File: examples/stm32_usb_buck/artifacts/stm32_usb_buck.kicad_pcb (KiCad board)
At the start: 4 copper layers, 90 x 58 mm, 28 parts, among them J2 SWD 10-pin, J3 GPIO 1x4, SW1 BOOT0, U1 STM32F405RGT6, Y1 8 MHz

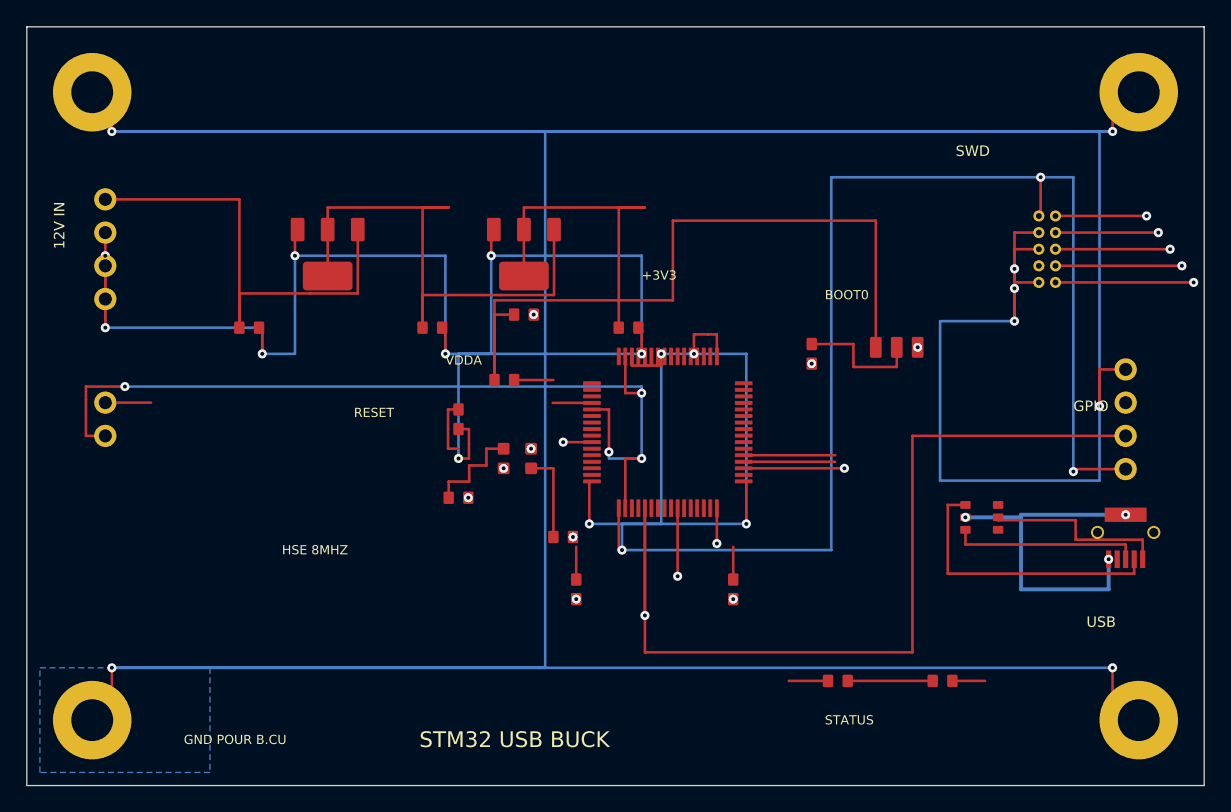
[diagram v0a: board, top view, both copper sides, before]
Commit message: Polish STM32 USB buck benchmark layout
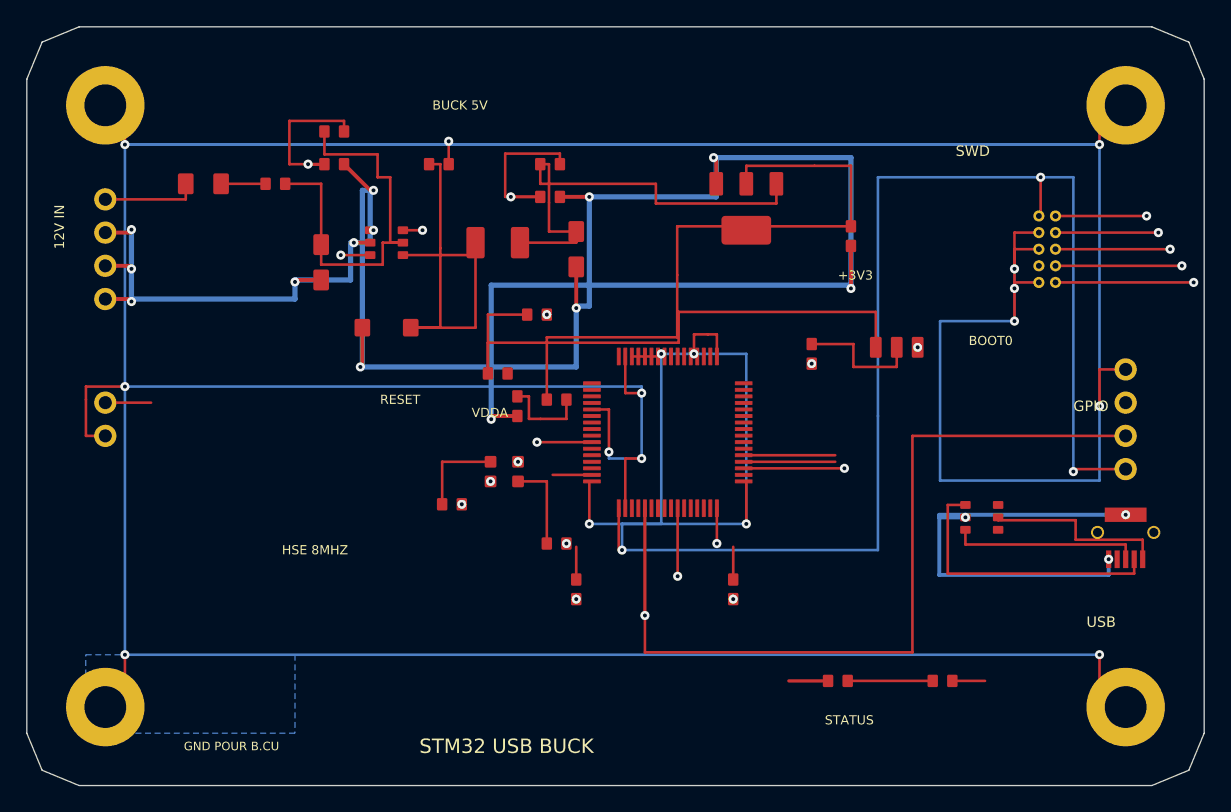
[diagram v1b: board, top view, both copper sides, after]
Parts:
- added C10: 18 pF, C_0603_1608Metric, F.Cu at (40.5, 39.5)
- added D2: Green LED, LED_0603_1608Metric, F.Cu at (70.0, 50.0)
- added H1: MountingHole_Pad, MountingHole_3.2mm_Pad_6.0mm, F.Cu at (6.00, 6.00)
- added H2: MountingHole_Pad, MountingHole_3.2mm_Pad_6.0mm, F.Cu at (84.0, 6.00)
- added H3: MountingHole_Pad, MountingHole_3.2mm_Pad_6.0mm, F.Cu at (6.00, 52.0)
- added H4: MountingHole_Pad, MountingHole_3.2mm_Pad_6.0mm, F.Cu at (84.0, 52.0)
- added J4: SWD 10-pin, PinHeader_2x05_P1.27mm_Vertical_SmallPads, F.Cu at (78.0, 17.0)
- added J5: GPIO 1x4, PinHeader_1x04_P2.54mm_Vertical, F.Cu at (84.0, 30.0)
- added R7: 330 Ohm, R_0603_1608Metric, F.Cu at (62.0, 50.0)
- added U1: STM32F405RGT6, LQFP-64_10x10mm_P0.5mm, F.Cu at (49.0, 31.0)
- C1: renamed from C4; value 100 nF -> 10 uF; footprint C_0603_1608Metric -> C_1206_3216Metric
- C2: renamed from USB/J1; value USB Micro-B -> 10 nF; footprint USB_Micro-B_Receptacle -> C_0603_1608Metric
- C3: renamed from USB/U1; value USBLC6-4SC6 -> 10 uF; footprint SOT-23-6 -> C_1206_3216Metric
- C4: renamed from SW1; value BOOT0 -> 4.7 uF; footprint SW_SPDT_PCM12 -> C_0603_1608Metric
- C5: renamed from C8; value 18 pF -> 100 nF
- C6: renamed from LED_STATUS/D; value Green LED -> 100 nF; footprint LED_0603_1608Metric -> C_0603_1608Metric
- C7: renamed from U1; value STM32F405RGT6 -> 2.2 uF; footprint LQFP-64_10x10mm_P0.5mm -> C_0603_1608Metric
- C8: renamed from J2; value SWD 10-pin -> 2.2 uF; footprint PinHeader_2x05_P1.27mm_Vertical_SmallPads -> C_0603_1608Metric
- C9: renamed from H4; value MountingHole_Pad -> 18 pF; footprint MountingHole_3.2mm_Pad_6.0mm -> C_0603_1608Metric
- D1: renamed from PWR/C3V3; value 4.7 uF -> B5819W; footprint C_0603_1608Metric -> D_SOD-123
- F1: renamed from PWR/U5; value AP1117-5.0 -> 250 mA polyfuse; footprint SOT-223-3_TabPin2 -> Fuse_1206_3216Metric
- FB1: renamed from PWR/U3V3; value AP1117-3.3 -> 600 Ohm @ 100 MHz; footprint SOT-223-3_TabPin2 -> L_0603_1608Metric
- FB2: renamed from Y1; value 8 MHz -> 600 Ohm @ 100 MHz; footprint Crystal_3225_4Pad -> L_0603_1608Metric
- J3: renamed from C9; value 18 pF -> USB Micro-B; footprint C_0603_1608Metric -> USB_Micro-B_Receptacle
- L1: renamed from PWR/C5V; value 4.7 uF -> 10 uH; footprint C_0603_1608Metric -> L_4.0x4.0mm
- R1: renamed from C5; value 100 nF -> 100 kOhm; footprint C_0603_1608Metric -> R_0603_1608Metric
- R2: renamed from C6; value 2.2 uF -> 47 kOhm; footprint C_0603_1608Metric -> R_0603_1608Metric
- R3: renamed from C7; value 2.2 uF -> 68 kOhm; footprint C_0603_1608Metric -> R_0603_1608Metric
- R4: renamed from R1; value 10 kOhm -> 15 kOhm
- R5: renamed from J3; value GPIO 1x4 -> 10 kOhm; footprint PinHeader_1x04_P2.54mm_Vertical -> R_0603_1608Metric
- R6: renamed from H1; value MountingHole_Pad -> 100 kOhm; footprint MountingHole_3.2mm_Pad_6.0mm -> R_0603_1608Metric
- SW1: renamed from H2; value MountingHole_Pad -> BOOT0; footprint MountingHole_3.2mm_Pad_6.0mm -> SW_SPDT_PCM12
- U2: renamed from PWR/CIN; value 4.7 uF -> MP2359 5V buck; footprint C_0603_1608Metric -> SOT-23-6
- U3: renamed from R2; value 100 kOhm -> AP1117-3.3; footprint R_0603_1608Metric -> SOT-223-3_TabPin2
- U4: renamed from LED_STATUS/R; value 330 Ohm -> USBLC6-4SC6; footprint R_0603_1608Metric -> SOT-23-6
- Y1: renamed from H3; value MountingHole_Pad -> 8 MHz; footprint MountingHole_3.2mm_Pad_6.0mm -> Crystal_3225_4Pad
- moved C2 59.7 mm to (31.5, 10.5), turned to 0 degrees
- moved R6 58.5 mm to (60.0, 25.0), turned to 90 degrees
- moved C9 55.0 mm to (32.5, 36.5)
- moved R5 48.1 mm to (36.0, 26.5), turned to 0 degrees
- moved J3 43.0 mm to (84.0, 39.0), turned to 180 degrees
- moved C6 41.8 mm to (39.0, 22.0)
- moved R2 37.4 mm to (23.5, 10.5), turned to 0 degrees
- moved C3 37.2 mm to (42.0, 17.0), turned to 90 degrees
- moved Y1 36.8 mm to (36.5, 34.0)
- moved R3 35.4 mm to (40.0, 10.5), turned to 0 degrees
- moved C8 35.4 mm to (54.0, 43.0), turned to 90 degrees
- moved SW1 26.9 mm to (66.5, 24.5)
- moved R1 20.2 mm to (23.5, 8.00)
- moved FB1 19.6 mm to (19.0, 12.0)
- moved D1 18.5 mm to (27.5, 23.0)
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- renumbered VIN_SRC to J1, PWR/J to J2
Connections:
- C1 pad 1: PWR/VDDA -> PWR/BUCK_IN
- C2 pad 1: USB/VBUS -> PWR/BUCK_SW
- C2 pad 2: USB/USB_DM -> PWR/BUCK_BST
- C3 pad 1: USB/USB_DP -> PWR/OUT_5V
- C3 pad 2: USB/GND -> PWR/GND
- C4 pad 1: SUPPORT/VDD -> PWR/OUT_3V3
- C4 pad 2: SUPPORT/BOOT0 -> PWR/GND
- C5 pad 1: SUPPORT/HSE_IN -> PWR/VDDA
- C5 pad 2: SUPPORT/GND -> PWR/GND
- C6 pad 1: LED_STATUS/SIGNAL -> SUPPORT/VDD
- C6 pad 2: LED_STATUS/GND -> SUPPORT/GND
- C7 pad 1: +3V3 -> SUPPORT/VCAP_1
- C7 pad 2: STATUS_LED -> SUPPORT/GND
- C8 pad 1: +3V3 -> SUPPORT/VCAP_2
- C8 pad 2: SWDIO -> SUPPORT/GND
- C9 pad 1: GND -> SUPPORT/HSE_IN
- D1 pad 1: PWR/OUT_3V3 -> PWR/GND
- D1 pad 2: PWR/GND -> PWR/BUCK_SW
- F1 pad 1: PWR/GND -> PWR/IN_12V
- F1 pad 2: PWR/OUT_5V -> PWR/FUSED_12V
- FB1 pad 1: PWR/GND -> PWR/FUSED_12V
- FB1 pad 2: PWR/OUT_3V3 -> PWR/BUCK_IN
- FB2 pad 1: SUPPORT/HSE_IN -> PWR/OUT_3V3
- FB2 pad 2: SUPPORT/GND -> PWR/VDDA
- J3 pad 1: SUPPORT/HSE_OUT -> USB/VBUS
- J3 pad 2: SUPPORT/GND -> USB/USB_DM
- L1 pad 1: PWR/OUT_5V -> PWR/BUCK_SW
- L1 pad 2: PWR/GND -> PWR/OUT_5V
- R1 pad 1: SUPPORT/VDD -> PWR/BUCK_IN
- R1 pad 2: SUPPORT/GND -> PWR/BUCK_EN
- R2 pad 1: SUPPORT/VCAP_1 -> PWR/BUCK_EN
- R2 pad 2: SUPPORT/GND -> PWR/GND
- R3 pad 1: SUPPORT/VCAP_2 -> PWR/OUT_5V
- R3 pad 2: SUPPORT/GND -> PWR/BUCK_FB
- R4 pad 1: SUPPORT/VDD -> PWR/BUCK_FB
- R4 pad 2: SUPPORT/NRST -> PWR/GND
- R5 pad 1: +3V3 -> SUPPORT/VDD
- R5 pad 2: BOOT0 -> SUPPORT/NRST
- R6 pad 1: GND -> SUPPORT/BOOT0
- SW1 pad 1: GND -> SUPPORT/VDD
- U2 pad 1: PWR/IN_12V -> PWR/BUCK_BST
- U3 pad 1: SUPPORT/BOOT0 -> PWR/GND
- U3 pad 2: SUPPORT/GND -> PWR/OUT_3V3
- U4 pad 1: LED_STATUS/SUPPLY -> USB/USB_DP
- U4 pad 2: LED_STATUS/SIGNAL -> USB/GND
- Y1 pad 1: GND -> SUPPORT/HSE_IN
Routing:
- net PWR/GND: track 121.7 -> 173.9 mm, vias 9 -> 12
- net PWR/BUCK_SW: track 0.00 -> 33.6 mm
- net PWR/BUCK_FB: track 0.00 -> 33.4 mm, vias 0 -> 2
- net PWR/BUCK_IN: track 0.00 -> 31.3 mm
- net PWR/IN_12V: track 36.6 -> 7.34 mm
- net PWR/BUCK_EN: track 0.00 -> 27.5 mm, vias 0 -> 2
- net PWR/OUT_3V3: track 25.7 -> 50.5 mm
- net PWR/BUCK_BST: track 0.00 -> 20.9 mm, vias 0 -> 2
- net SUPPORT/VDD: track 57.5 -> 44.6 mm
- net GND: track 516.8 -> 506.8 mm
- net USB/GND: track 27.0 -> 35.0 mm
- net PWR/OUT_5V: track 43.2 -> 35.6 mm
- net LED_STATUS/LED_A: track 0.00 -> 6.50 mm
- net NRST: track 103.7 -> 107.7 mm
- net LED_STATUS/SIGNAL: track 6.50 -> 2.50 mm
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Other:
- outline, holes or cut-outs redrawn
- board text added: "BUCK 5V"

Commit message: Address STM32 USB buck review findings
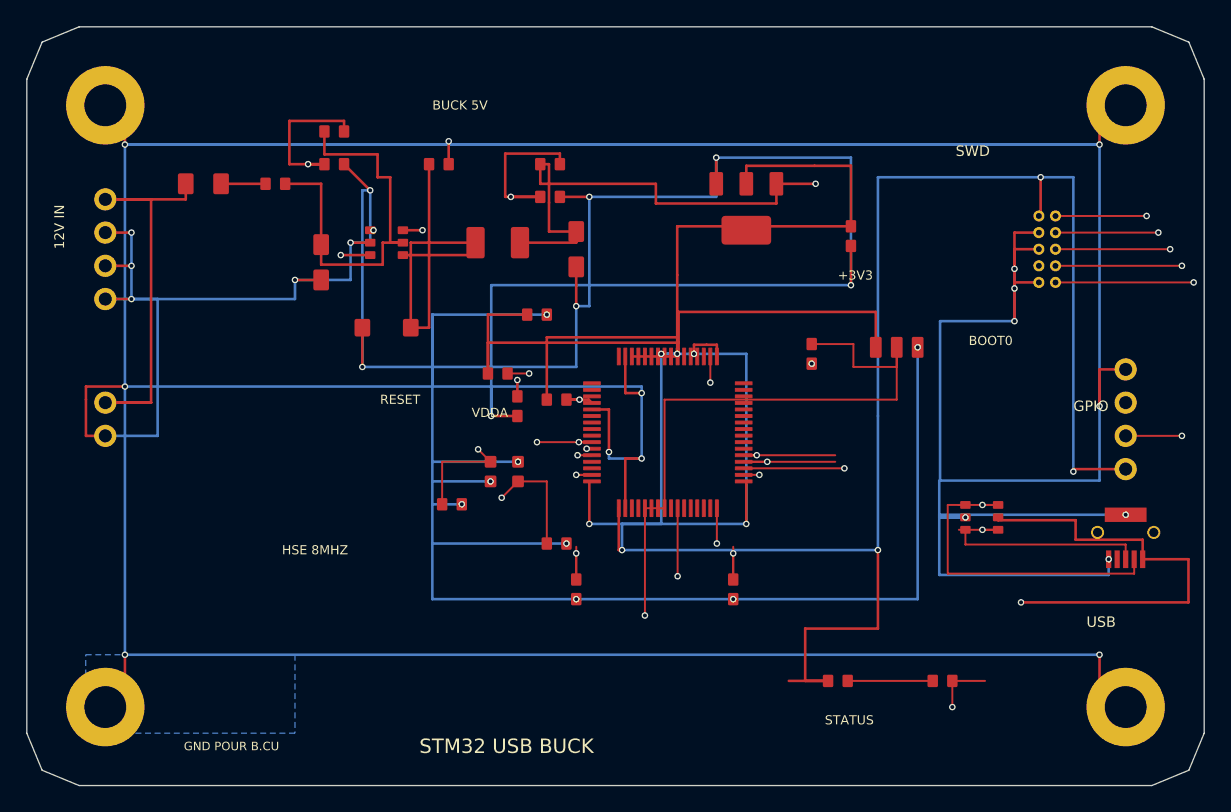
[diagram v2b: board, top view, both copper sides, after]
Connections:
- C1 pad 2: PWR/GND -> GND
- C10 pad 2: SUPPORT/GND -> GND
- C3 pad 1: PWR/OUT_5V -> +5V
- C3 pad 2: PWR/GND -> GND
- C4 pad 1: PWR/OUT_3V3 -> +3V3
- C4 pad 2: PWR/GND -> GND
- C5 pad 1: PWR/VDDA -> VDDA
- C5 pad 2: PWR/GND -> GND
- C6 pad 1: SUPPORT/VDD -> +3V3
- C6 pad 2: SUPPORT/GND -> GND
- C7 pad 2: SUPPORT/GND -> GND
- C8 pad 2: SUPPORT/GND -> GND
- C9 pad 2: SUPPORT/GND -> GND
- D1 pad 1: PWR/GND -> GND
- D2 pad 2: LED_STATUS/SIGNAL -> STATUS_LED
- F1 pad 1: PWR/IN_12V -> +12V
- FB2 pad 1: PWR/OUT_3V3 -> +3V3
- FB2 pad 2: PWR/VDDA -> VDDA
- J2 pad 1: PWR/IN_12V -> +12V
- J2 pad 2: PWR/GND -> GND
- J2 pad 3: PWR/GND -> GND
- J2 pad 4: PWR/GND -> GND
- J3 pad 1: USB/VBUS -> +5V
- J3 pad 2: USB/USB_DM -> USB_DM
- J3 pad 3: USB/USB_DP -> USB_DP
- J3 pad 5: USB/GND -> GND
- J3 pad 6: USB/GND -> GND
- J4 pad 10: NRST -> SUPPORT/NRST
- J4 pad 8: BOOT0 -> SUPPORT/BOOT0
- J5 pad 2: BOOT0 -> SUPPORT/BOOT0
- L1 pad 2: PWR/OUT_5V -> +5V
- R2 pad 2: PWR/GND -> GND
- R3 pad 1: PWR/OUT_5V -> +5V
- R4 pad 2: PWR/GND -> GND
- R5 pad 1: SUPPORT/VDD -> +3V3
- R6 pad 2: SUPPORT/GND -> GND
- R7 pad 1: LED_STATUS/SUPPLY -> +3V3
- SW1 pad 1: SUPPORT/VDD -> +3V3
- SW1 pad 3: SUPPORT/GND -> GND
- U1 pad 31: VCAP_1 -> SUPPORT/VCAP_1
- U1 pad 44: MCU_USB_DM -> USB_DM
- U1 pad 45: MCU_USB_DP -> USB_DP
- U1 pad 47: VCAP_2 -> SUPPORT/VCAP_2
- U1 pad 5: HSE_IN -> SUPPORT/HSE_IN
- U1 pad 6: HSE_OUT -> SUPPORT/HSE_OUT
- U1 pad 60: BOOT0 -> SUPPORT/BOOT0
- U1 pad 7: NRST -> SUPPORT/NRST
- U2 pad 2: PWR/GND -> GND
- U3 pad 1: PWR/GND -> GND
- U3 pad 2: PWR/OUT_3V3 -> +3V3
- U3 pad 3: PWR/OUT_5V -> +5V
- U3 pad 4: PWR/OUT_3V3 -> +3V3
- U4 pad 1: USB/USB_DP -> USB_DP
- U4 pad 2: USB/GND -> GND
- U4 pad 3: USB/USB_DM -> USB_DM
- U4 pad 4: USB/MCU_USB_DM -> USB_DM
- U4 pad 5: USB/VBUS -> +5V
- U4 pad 6: USB/MCU_USB_DP -> USB_DP
- Y1 pad 2: SUPPORT/GND -> GND
- Y1 pad 4: SUPPORT/GND -> GND
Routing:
- net GND: track 506.8 -> 888.7 mm, vias 12 -> 36
- net PWR/GND: track 173.9 -> 0.00 mm, vias 12 -> 0
- net BOOT0: track 150.0 -> 0.00 mm, vias 2 -> 0
- net +5V: track 0.00 -> 145.8 mm, vias 0 -> 2
- net SUPPORT/BOOT0: track 9.75 -> 131.2 mm, vias 0 -> 3
- net SUPPORT/NRST: track 0.00 -> 118.8 mm, vias 0 -> 4
- net +3V3: track 160.0 -> 278.7 mm, vias 7 -> 9
- net SUPPORT/GND: track 110.3 -> 0.00 mm, vias 9 -> 0
- net NRST: track 107.7 -> 0.00 mm, vias 2 -> 0
- net STATUS_LED: track 3.00 -> 81.2 mm, vias 0 -> 2
- net USB_DM: track 0.00 -> 57.7 mm, vias 0 -> 2
- net USB_DP: track 0.00 -> 53.2 mm, vias 0 -> 2
- net PWR/OUT_3V3: track 50.5 -> 0.00 mm
- net SUPPORT/VDD: track 44.6 -> 0.00 mm
- net PWR/OUT_5V: track 35.6 -> 0.00 mm
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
